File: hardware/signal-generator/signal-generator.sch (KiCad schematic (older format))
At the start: 10 parts

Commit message: [Signal Generator] Layout microcontroller and allocate its pins
The microcontroller is the brains of the function generator system - it
is responsible for controlling the DDS signal generator system, as well
as the LCD module which provides the user interface. The specific
microcontroller used in this project is the ATmega2561-16AU from the
megaAVR uC family. The reasons I have picked this particular part are
the following:
- I am familiar with the AVR uC structure;
- it provides more SRAM memory (8 kB) than other MCUs of the same family;
- it has fewer pins (and therefore peripherals) than the ATmega2560.
Only a fraction of the available peripheral pins of the ATmega2561 have
been utilized in the current design. The remaining port pins (which are
internally connected to useful peripherals such as JTAG, XMEM, etc.)
are connected to pin header connectors and are meant for
upgrading/modifying the system as a whole by including additional
external circuitry. The ATmega2561's SPI port is also connected to a
similar pin header connector which allows the uC to play the role of an
SPI slave device.
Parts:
- removed C? (x2): 2.2uF, symbol Device:C
- removed U?: ADP7182AUZJ-5.0, Package_TO_SOT_SMD:TSOT-23-5, symbol Regulator_Linear:ADP7182AUZJ
- added C? (x3): 100nF, symbol Device:C
- added C? (x2): 22pF, symbol Device:C
- added C?: 330nF, symbol Device:C
- added D?: CD1206-SO1575, symbol Device:D
- added J?: AVR-ISP-6, symbol Connector:AVR-ISP-6
- added J?: Output_Conn, symbol Connector:Conn_Coaxial
- added J?: PORT_A, symbol Connector_Generic:Conn_01x08
- added J?: PORT_C, symbol Connector_Generic:Conn_01x08
- added J?: PORT_G, symbol Connector_Generic:Conn_01x06
- added J?: PORT_F, symbol Connector_Generic:Conn_01x04
- added J?: AVR_SPI, symbol Connector_Generic:Conn_01x04
- added J?: PORT_E, symbol Connector_Generic:Conn_01x08
- added J?: AREF, symbol Connector_Generic:Conn_01x01
- added R?: 10k, symbol Device:R
- added R?: 1M, symbol Device:R
- added R? (x2): 2k, symbol Device:R
- added SW?: RESET_BUTTON, symbol Switch:SW_Push
- added U?: ATmega2561-16AU, Package_QFP:TQFP-64_14x14mm_P0.8mm, symbol MCU_Microchip_ATmega:ATmega2561-16AU
- added U?: L78L33_SO8, Package_SO:SOIC-8_3.9x4.9mm_P1.27mm, symbol Regulator_Linear:L78L33_SO8
- added U?: 74HC04, symbol 74xx:74HC04
- added Y?: 16MHz, symbol Device:Crystal
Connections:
- net labels added: +3.3V, DC\~RS~_LCD, IOExINTA, IOExINTB, IRQ_T, MISO, MOSI, PWRDWN\~SS, R\~W, SCK, SCL, SDA, XTAL1, XTAL2, ~CMR1, ~CMR2, ~CP, ~CS~_LCD, ~CS~_SD, ~CS~_T, ~IOExRESET, ~OSCOE, ~RESET, ~RESET~_LCD
- net labels removed: -5VA
- wire segments 62 -> 201
- no-connect marks 3 -> 2
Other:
- note added: "+3.3VD RAIL"
- note added: "+5VA RAIL"
- note added: "AVR SPI INTERFACE"
- note added: "CRYSTAL OSCILLATOR"
- note added: "DEBUG/PROGRAM"
- note added: "Microcontroller"
- note added: "RESET BUTTON"
- note added: "WAVEFORM PROCESSING CIRCUITRY"
- note removed: "+5VA/-5VA RAILS"
- moved on the sheet: C?, J?, U?

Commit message: [Signal Generator] Place unused logic gates and logic IC supplies
Both of these elements can be located on the main project sheet
('signal-generator.sch').
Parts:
- added C? (x4): 100nF, symbol Device:C
- added U?: 74HC30, Housings_SOIC:SOIC-14_3.9x8.7mm_Pitch1.27mm, symbol ulib_MY_74xx:74HC30
- added U? (x4): 74HC08, Housings_SOIC:SOIC-14_3.9x8.7mm_Pitch1.27mm, symbol ulib_MY_74xx:74HC08
- added U? (x4): 74HC04, symbol 74xx:74HC04
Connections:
- wire segments 201 -> 225
- no-connect marks 2 -> 14
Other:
- note added: "LOGIC IC POWER SUPPLIES"
- note added: "MICROCONTROLLER"
- note added: "UNUSED LOGIC GATES"
- note removed: "Microcontroller"
- moved on the sheet: C?, D?, J?, R?, SW?, U?, Y?

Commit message: [Signal Generator] Add DAC output conversion stage
The additional opamp stage is a differential amplifier configuration
which converts the differential current outputs of the DAC to a singular
voltage output in the range -0.5V to +0.5V.

The electrical schematic has overall been finalized with this addition.
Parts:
- removed J?: PORT_F, symbol Connector_Generic:Conn_01x04
- added J?: PORT_F, symbol Connector_Generic:Conn_01x05
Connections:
- net labels added: PWRDWN, ~SS
- net labels removed: IOExINTA, IOExINTB, PWRDWN\~SS
- wire segments 225 -> 229
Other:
- moved on the sheet: C?, J?, U?

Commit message: [Signal Generator] Implement +3.3VD line with TC1017 voltage regulator
Up until now, the +3.3VD line was implemented using the L78L33 linear
voltage regulator. However, the latter has a dropout voltage of 2V which
means that the L78L33 cannot output a stable +3.3V from a +5V input.

To solve the aforementioned problem the TC1017 LDO voltage regulator has
replaced the L78L33. The former has a low dropout voltage of 180mV (typ.) at
100mA load current.
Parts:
- removed U?: L78L33_SO8, Package_SO:SOIC-8_3.9x4.9mm_P1.27mm, symbol Regulator_Linear:L78L33_SO8
- added U?: TC1017-3.3CTTR, Package_TO_SOT_SMD:SOT-23-5, symbol Regulator_Linear:TC1017-xCT
- C? (x3): footprint (none) -> Capacitors_SMD:CP_Elec_4x5.3
- C? (x2): footprint (none) -> Capacitors_SMD:C_0805_HandSoldering
- C? (x8): footprint (none) -> Capacitors_SMD:C_1206_HandSoldering
- C?: value 330nF -> 1uF; footprint (none) -> Capacitors_SMD:C_1206_HandSoldering
- C?: value 100nF -> 1uF; footprint (none) -> Capacitors_SMD:C_1206_HandSoldering
- D?: footprint (none) -> Diodes_SMD:D_1206
- J?: footprint (none) -> Pin_Headers:Pin_Header_Straight_2x05_Pitch2.54mm
- J?: footprint (none) -> Pin_Headers:Pin_Header_Straight_2x03_Pitch2.54mm
- J?: footprint (none) -> Connectors_TE-Connectivity:BNC_Socket_TYCO-AMP
- J?: footprint (none) -> Pin_Headers:Pin_Header_Straight_1x05_Pitch2.54mm
- J? (x3): footprint (none) -> Pin_Headers:Pin_Header_Straight_1x08_Pitch2.54mm
- J?: footprint (none) -> Pin_Headers:Pin_Header_Straight_1x06_Pitch2.54mm
- J?: footprint (none) -> Pin_Headers:Pin_Header_Straight_1x04_Pitch2.54mm
- J?: footprint (none) -> Pin_Headers:Pin_Header_Straight_1x01_Pitch2.54mm
- R? (x4): footprint (none) -> Resistors_SMD:R_1206_HandSoldering
- SW?: footprint (none) -> Buttons_Switches_THT:SW_PUSH_6mm_h4.3mm
- U?: footprint Package_TO_SOT_SMD:TSOT-23-5 -> TO_SOT_Packages_SMD:TSOT-23-5_HandSoldering
- U?: footprint Package_QFP:TQFP-64_14x14mm_P0.8mm -> Housings_QFP:TQFP-64_14x14mm_Pitch0.8mm
- U? (x5): footprint (none) -> Housings_SOIC:SOIC-14_3.9x8.7mm_Pitch1.27mm
- Y?: footprint (none) -> Crystals:Crystal_HC49-U_Vertical
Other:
- moved on the sheet: C?

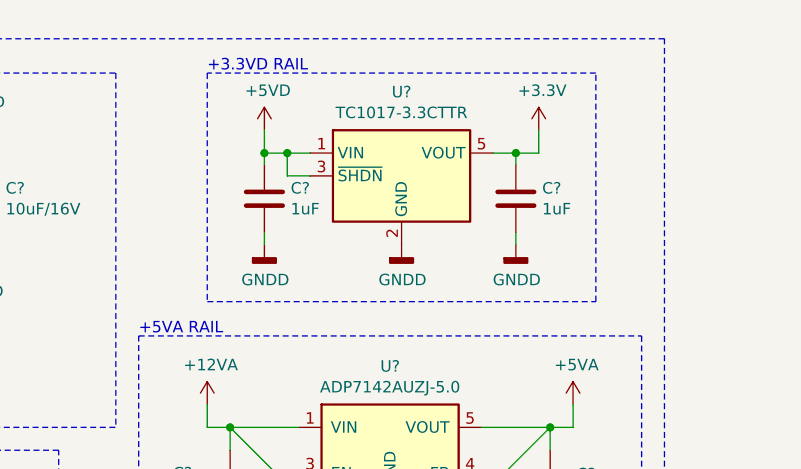
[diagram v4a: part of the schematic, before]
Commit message: [Signal Generator] Power the LCD module with the +5VD rail
Previously, the LCD module was powered via the +3.3VD rail. The module itself
consumes about 90mA and the level shifters may consume  >= 50mA in worst
case scenarios. Looking at the module's (MSP3218) schematic, it can be
observed that the VCC line is connected to the XC6206 +3.3V LDO voltage
regulator. Therefore, I have decided to power the module from the +5VD
supply rail which is external to the board (as opposed to the +3.3VD
rail which resides entirely on the digital function generator's PCB).
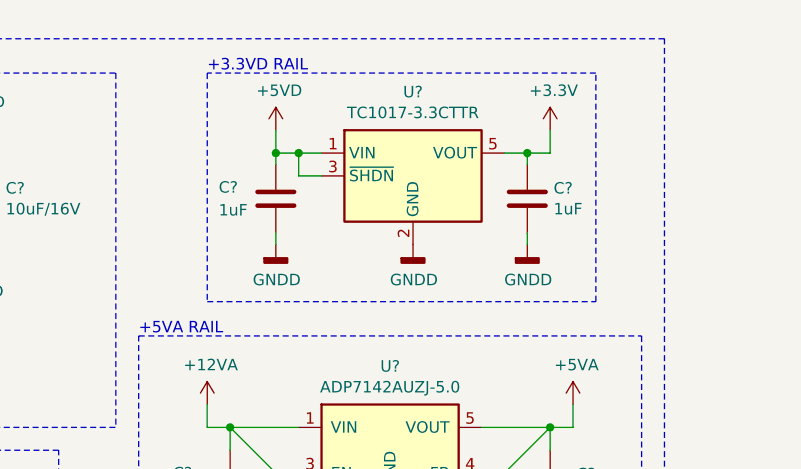
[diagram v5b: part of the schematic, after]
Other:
- moved on the sheet: C?, U?
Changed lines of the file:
@@
 L power:GNDD #PWR0123
 U 1 1 5DDFA816
-P 9350 1500
-F 0 "#PWR0123" H 9350 1250 50  0001 C CNN
-F 1 "GNDD" H 9354 1345 50  0000 C CNN
-F 2 "" H 9350 1500 50  0001 C CNN
-F 3 "" H 9350 1500 50  0001 C CNN
-	1    9350 1500
+P 9400 1500
+F 0 "#PWR0123" H 9400 1250 50  0001 C CNN
+F 1 "GNDD" H 9404 1345 50  0000 C CNN
+F 2 "" H 9400 1500 50  0001 C CNN
+F 3 "" H 9400 1500 50  0001 C CNN
+	1    9400 1500
 	1    0    0    -1
 $EndComp
@@
 L Device:C C?
 U 1 1 5DDFA8DE
-P 8750 1300
-F 0 "C?" H 8865 1346 50  0000 L CNN
-F 1 "1uF" H 8865 1255 50  0000 L CNN
-F 2 "Capacitors_SMD:C_1206_HandSoldering" H 8788 1150 50  0001 C CNN
-F 3 "~" H 8750 1300 50  0001 C CNN
-	1    8750 1300
+P 8800 1300
+F 0 "C?" H 8550 1350 50  0000 L CNN
+F 1 "1uF" H 8550 1250 50  0000 L CNN
+F 2 "Capacitors_SMD:C_1206_HandSoldering" H 8838 1150 50  0001 C CNN
+F 3 "~" H 8800 1300 50  0001 C CNN
+	1    8800 1300
 	1    0    0    -1
 $EndComp
@@
 L power:GNDD #PWR0124
 U 1 1 5DE0450F
-P 9850 1500
-F 0 "#PWR0124" H 9850 1250 50  0001 C CNN
-F 1 "GNDD" H 9854 1345 50  0000 C CNN
-F 2 "" H 9850 1500 50  0001 C CNN
-F 3 "" H 9850 1500 50  0001 C CNN
-	1    9850 1500
+P 9900 1500
+F 0 "#PWR0124" H 9900 1250 50  0001 C CNN
+F 1 "GNDD" H 9904 1345 50  0000 C CNN
+F 2 "" H 9900 1500 50  0001 C CNN
+F 3 "" H 9900 1500 50  0001 C CNN
+	1    9900 1500
 	1    0    0    -1
 $EndComp
@@
 L power:GNDD #PWR0125
 U 1 1 5DE07AD1
-P 8750 1500
-F 0 "#PWR0125" H 8750 1250 50  0001 C CNN
-F 1 "GNDD" H 8754 1345 50  0000 C CNN
-F 2 "" H 8750 1500 50  0001 C CNN
-F 3 "" H 8750 1500 50  0001 C CNN
-	1    8750 1500
+P 8800 1500
+F 0 "#PWR0125" H 8800 1250 50  0001 C CNN
+F 1 "GNDD" H 8804 1345 50  0000 C CNN
+F 2 "" H 8800 1500 50  0001 C CNN
+F 3 "" H 8800 1500 50  0001 C CNN
+	1    8800 1500
 	1    0    0    -1
 $EndComp
@@
 L power:+3.3V #PWR0126
 U 1 1 5DE1BC69
-P 9950 1000
-F 0 "#PWR0126" H 9950 850 50  0001 C CNN
-F 1 "+3.3V" H 9965 1173 50  0000 C CNN
-F 2 "" H 9950 1000 50  0001 C CNN
-F 3 "" H 9950 1000 50  0001 C CNN
-	1    9950 1000
+P 10000 1000
+F 0 "#PWR0126" H 10000 850 50  0001 C CNN
+F 1 "+3.3V" H 10015 1173 50  0000 C CNN
+F 2 "" H 10000 1000 50  0001 C CNN
+F 3 "" H 10000 1000 50  0001 C CNN
+	1    10000 1000
 	1    0    0    -1
 $EndComp
@@
 L power:+5VD #PWR0127
 U 1 1 5DE1F4E9
-P 8750 1000
-F 0 "#PWR0127" H 8750 850 50  0001 C CNN
-F 1 "+5VD" H 8765 1173 50  0000 C CNN
-F 2 "" H 8750 1000 50  0001 C CNN
-F 3 "" H 8750 1000 50  0001 C CNN
-	1    8750 1000
+P 8800 1000
+F 0 "#PWR0127" H 8800 850 50  0001 C CNN
+F 1 "+5VD" H 8815 1173 50  0000 C CNN
+F 2 "" H 8800 1000 50  0001 C CNN
+F 3 "" H 8800 1000 50  0001 C CNN
+	1    8800 1000
 	1    0    0    -1
 $EndComp
@@
 L Regulator_Linear:TC1017-xCT U?
 U 1 1 5DF612CD
-P 9350 1200
-F 0 "U?" H 9350 1567 50  0000 C CNN
-F 1 "TC1017-3.3CTTR" H 9350 1476 50  0000 C CNN
-F 2 "Package_TO_SOT_SMD:SOT-23-5" H 9100 1550 50  0001 L CIN
-F 3 "http://ww1.microchip.com/downloads/en/DeviceDoc/21813F.pdf" H 9350 1100 50  0001 C CNN
-	1    9350 1200
-	1    0    0    -1
-$EndComp
-Wire Wire Line
-	9950 1000 9950 1100
-Wire Wire Line
-	9950 1100 9850 1100
-Wire Wire Line
-	9850 1150 9850 1100
-Connection ~ 9850 1100
-Wire Wire Line
-	9850 1100 9750 1100
+P 9400 1200
+F 0 "U?" H 9400 1567 50  0000 C CNN
+F 1 "TC1017-3.3CTTR" H 9400 1476 50  0000 C CNN
+F 2 "Package_TO_SOT_SMD:SOT-23-5" H 9150 1550 50  0001 L CIN
+F 3 "http://ww1.microchip.com/downloads/en/DeviceDoc/21813F.pdf" H 9400 1100 50  0001 C CNN
+	1    9400 1200
+	1    0    0    -1
+$EndComp
+Wire Wire Line
+	10000 1000 10000 1100
+Wire Wire Line
+	10000 1100 9900 1100
+Wire Wire Line
+	9900 1150 9900 1100
+Connection ~ 9900 1100
+Wire Wire Line
+	9900 1100 9800 1100
 $Comp
 L Device:C C?
 U 1 1 5DDFDC52
-P 9850 1300
-F 0 "C?" H 9965 1346 50  0000 L CNN
-F 1 "1uF" H 9965 1255 50  0000 L CNN
-F 2 "Capacitors_SMD:C_1206_HandSoldering" H 9888 1150 50  0001 C CNN
-F 3 "~" H 9850 1300 50  0001 C CNN
-	1    9850 1300
-	1    0    0    -1
-$EndComp
-Wire Wire Line
-	8950 1100 8850 1100
-Wire Wire Line
-	8750 1100 8750 1000
-Wire Wire Line
-	9850 1500 9850 1450
-Wire Wire Line
-	8950 1200 8850 1200
-Connection ~ 8850 1100
-Wire Wire Line
-	8850 1100 8750 1100
-Wire Wire Line
-	8850 1100 8850 1200
-Wire Wire Line
-	8750 1150 8750 1100
-Connection ~ 8750 1100
-Wire Wire Line
-	8750 1500 8750 1450
+P 9900 1300
+F 0 "C?" H 10015 1346 50  0000 L CNN
+F 1 "1uF" H 10015 1255 50  0000 L CNN
+F 2 "Capacitors_SMD:C_1206_HandSoldering" H 9938 1150 50  0001 C CNN
+F 3 "~" H 9900 1300 50  0001 C CNN
+	1    9900 1300
+	1    0    0    -1
+$EndComp
+Wire Wire Line
+	9000 1100 8900 1100
+Wire Wire Line
+	8800 1100 8800 1000
+Wire Wire Line
+	9900 1500 9900 1450
+Wire Wire Line
+	9000 1200 8900 1200
+Connection ~ 8900 1100
+Wire Wire Line
+	8900 1100 8800 1100
+Wire Wire Line
+	8900 1100 8900 1200
+Wire Wire Line
+	8800 1150 8800 1100
+Connection ~ 8800 1100
+Wire Wire Line
+	8800 1500 8800 1450
 $EndSCHEMATC

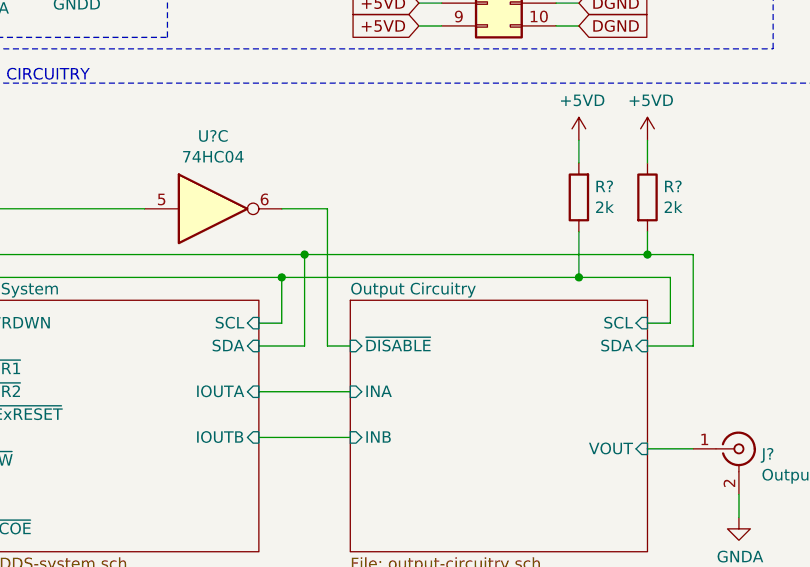
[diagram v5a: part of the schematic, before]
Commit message: [Signal Generator] Use external reference for DAC. Change MCP23017's I2C address
The DDS system's DAC (AD9764 or any other from the TxDAC family)
previously was set up to use its internal 1.2V reference. However, due
to production tolerances, this reference is quite inaccurate ranging
from 1.08V to 1.32V (taken from the AD9764's datasheet). Since this
inaccuracy would greatly affect the generator's precision, I have
decided to use an external voltage reference. Said reference is
generated by the TC4061A which produces a very accurate (0.1% deviation)
1.25V reference.

Also, the I/O expander's (MCP23017's) I2C address has been changed from
'0100 111' to '0100 000'.
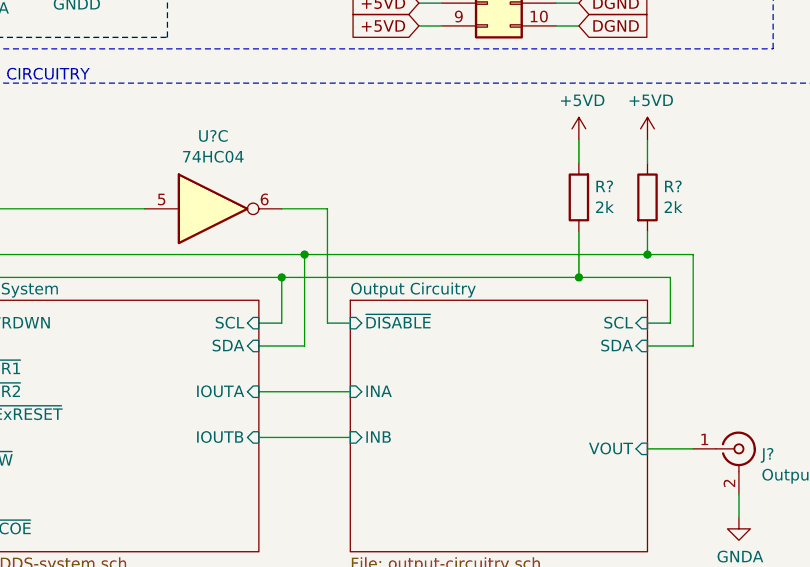
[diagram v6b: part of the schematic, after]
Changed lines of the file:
@@
 F0 "Output Circuitry" 50
 F1 "output-circuitry.sch" 50
-F2 "~DISABLE" I L 8650 5200 50
+F2 "~DISABLE" I L 8650 5100 50
 F3 "VOUT" I R 9950 5650 50
 F4 "SDA" I R 9950 5200 50
@@
 	9650 4400 9650 4300
 Wire Wire Line
-	8650 5200 8550 5200
+	8650 5100 8550 5100
 $Comp
 L 74xx:74HC04 U?
@@
 	8350 4600 8550 4600
 Wire Wire Line
-	8550 4600 8550 5200
+	8550 4600 8550 5100
 Wire Wire Line
 	7750 4600 6850 4600
